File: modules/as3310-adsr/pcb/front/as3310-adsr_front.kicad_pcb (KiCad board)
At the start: 2 copper layers, 18.3 x 107.4 mm, 22 parts, among them J1 Pin Header 1x9, J2 Thonkiconn SM, J3 Thonkiconn SM

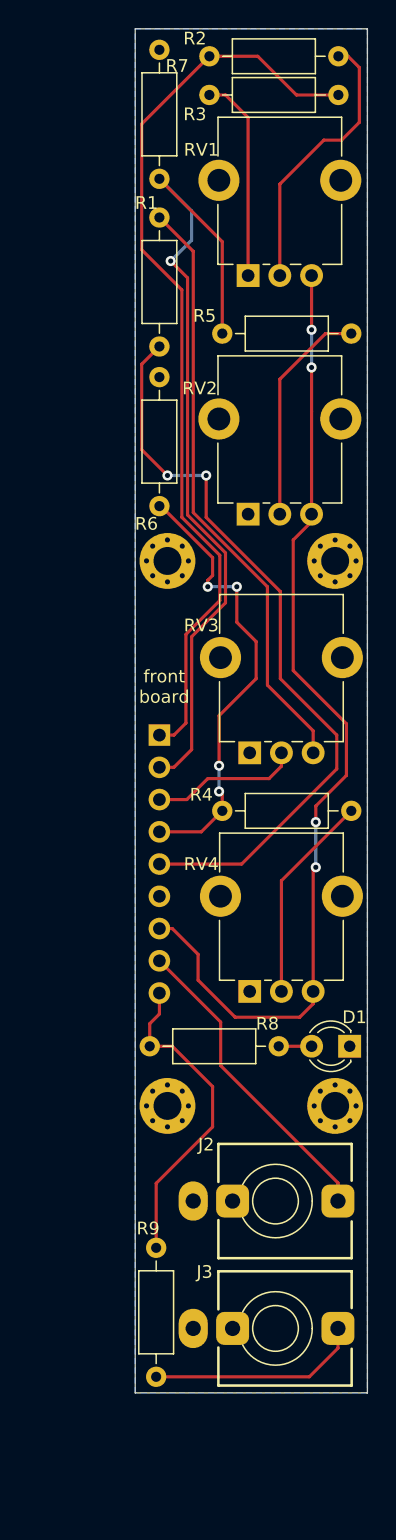
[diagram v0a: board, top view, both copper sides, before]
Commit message: modules: as3310-adsr: front: revision A (redesign)
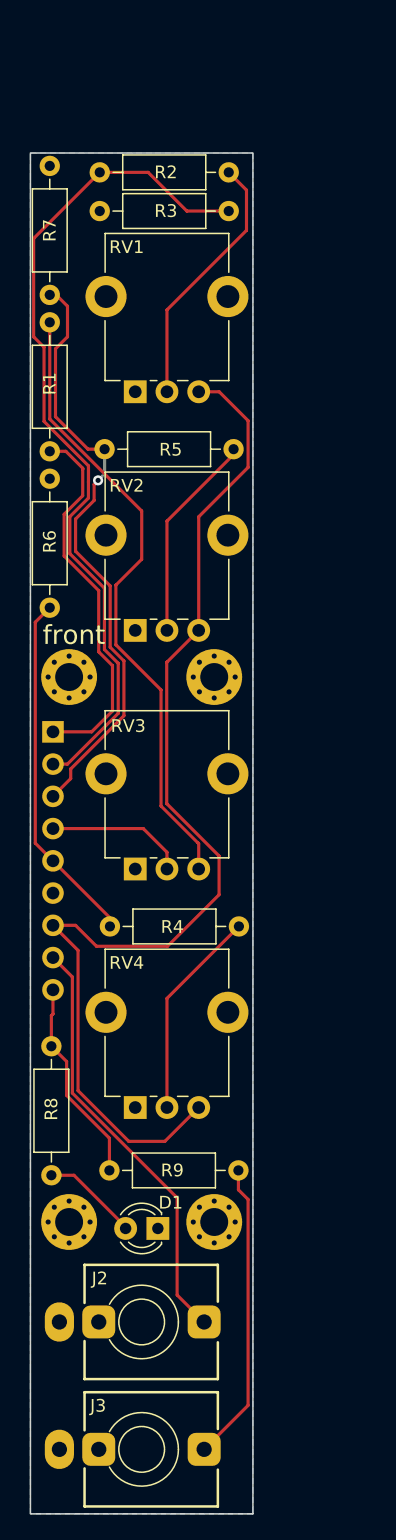
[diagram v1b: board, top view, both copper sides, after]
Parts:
- added REF**: Eurorack_PCB_4HP, eurorack:Eurorack_PCB_4HP, F.Cu at (147.2, 103.8)
- D1: footprint eurorack:LED_D3.0mmP2.54mm -> LED_THT:LED_D3.0mm
- moved REF** 70.7 mm to (149.0, 56.3)
- moved D1 20.8 mm to (148.5, 134.9)
- moved J2 14.2 mm to (147.2, 142.2)
- moved J3 14.2 mm to (147.2, 152.3)
- moved H4 13.2 mm to (152.9, 134.4)
- moved H2 13.2 mm to (152.9, 91.4)
- moved R5 13.0 mm to (154.4, 73.5)
- moved RV3 12.8 mm to (146.7, 106.6)
- moved RV4 12.8 mm to (146.7, 125.3)
- moved RV1 12.8 mm to (146.7, 69.0)
- moved RV2 12.8 mm to (146.7, 87.8)
- moved R4 12.7 mm to (154.9, 111.1)
- moved R2 12.6 mm to (154.1, 51.7)
- moved R3 12.6 mm to (154.1, 54.7)
- moved R7 12.6 mm to (140.0, 61.3)
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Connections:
- H1 pad 1: (no net) -> GND
- H2 pad 1: (no net) -> GND
- H3 pad 1: (no net) -> GND
- H4 pad 1: (no net) -> GND
- J1 pad 1: ATTACK -> +12V
- J1 pad 2: DECAY -> ATTACK
- J1 pad 3: SUSTAIN -> DECAY
- J1 pad 4: RELEASE -> SUSTAIN
- J1 pad 5: +12V -> RELEASE
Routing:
- net +12V: track 59.1 -> 29.8 mm, vias 2 -> 0
- net DECAY: track 66.9 -> 48.0 mm
- net GND: track 16.2 -> 0.00 mm
- net -12V: track 77.4 -> 88.1 mm, vias 4 -> 0
- net OUT: track 25.3 -> 16.2 mm
- net GATE: track 24.7 -> 33.6 mm
- net RELEASE: track 35.8 -> 28.0 mm, vias 4 -> 0
- net Net-(J3-PadT): track 16.8 -> 23.7 mm
- net ATTACK: track 72.3 -> 67.0 mm
- net Net-(D1-Pad2): track 2.59 -> 7.65 mm
- net Net-(R1-Pad2): track 47.2 -> 49.6 mm
- net Net-(R2-Pad1): track 21.8 -> 20.5 mm
- net Net-(R5-Pad1): track 17.7 -> 16.6 mm
- net SUSTAIN: track 11.8 -> 11.1 mm
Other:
- board size 18.3 x 107.4 mm -> 17.5 x 107.2 mm
- board text added: "as3310 adsr Rev. A"
- board text added: "front"
- board text removed: "AS3310-VCO r1.0"
- board text removed: "front board"
